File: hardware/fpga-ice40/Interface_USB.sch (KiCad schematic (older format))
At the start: 14 parts, among them J5 USB_B_Micro, U11 USBLC6-2SC6, U9 FT245RL

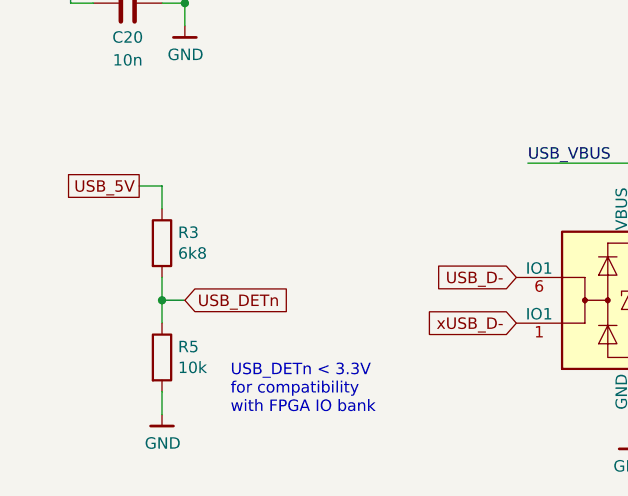
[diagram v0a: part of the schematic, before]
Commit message: Routed N64, DRAM, FIFO, and SD card interfaces
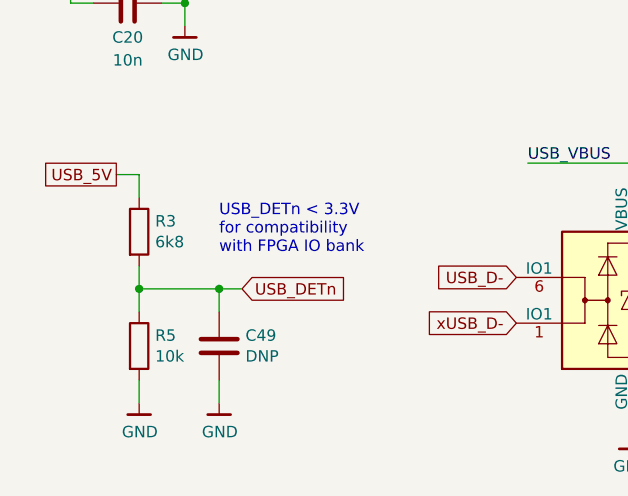
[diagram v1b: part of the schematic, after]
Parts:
- added C49: DNP, Capacitor_SMD:C_0603_1608Metric, symbol Device:C
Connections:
- net GND: now also C49.2
- net USB_DETn: now also C49.1
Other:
- moved on the sheet: R3, R5
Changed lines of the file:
@@
 L Device:R R?
 U 1 1 5F3148AD
-P 3150 4500
+P 3050 4450
 AR Path="/5F3148AD" Ref="R?"  Part="1"
 AR Path="/5F302051/5F3148AD" Ref="R3"  Part="1"
-F 0 "R3" H 3220 4546 50  0000 L CNN
-F 1 "6k8" H 3220 4455 50  0000 L CNN
-F 2 "Resistor_SMD:R_0603_1608Metric" V 3080 4500 50  0001 C CNN
-F 3 "~" H 3150 4500 50  0001 C CNN
-F 4 "RC0603FR-076K8L" H 3150 4500 50  0001 C CNN "MPN"
-	1    3150 4500
-	1    0    0    -1
-$EndComp
-$Comp
-L Device:R R?
-U 1 1 5F3148B3
-P 3150 5000
-AR Path="/5F3148B3" Ref="R?"  Part="1"
-AR Path="/5F302051/5F3148B3" Ref="R5"  Part="1"
-F 0 "R5" H 3220 5046 50  0000 L CNN
-F 1 "10k" H 3220 4955 50  0000 L CNN
-F 2 "Resistor_SMD:R_0603_1608Metric" V 3080 5000 50  0001 C CNN
-F 3 "~" H 3150 5000 50  0001 C CNN
-F 4 "RC0603FR-0710KL" H 3150 5000 50  0001 C CNN "MPN"
-	1    3150 5000
-	1    0    0    -1
-$EndComp
-Wire Wire Line
-	3150 5150 3150 5250
+F 0 "R3" H 3120 4496 50  0000 L CNN
+F 1 "6k8" H 3120 4405 50  0000 L CNN
+F 2 "Resistor_SMD:R_0603_1608Metric" V 2980 4450 50  0001 C CNN
+F 3 "~" H 3050 4450 50  0001 C CNN
+F 4 "RC0603FR-076K8L" H 3050 4450 50  0001 C CNN "MPN"
+	1    3050 4450
+	1    0    0    -1
+$EndComp
+Wire Wire Line
+	3050 5100 3050 5200
 $Comp
 L ng_power:GND #PWR?
 U 1 1 5F3148BA
-P 3150 5250
+P 3050 5200
 AR Path="/5F3148BA" Ref="#PWR?"  Part="1"
 AR Path="/5F302051/5F3148BA" Ref="#PWR024"  Part="1"
-F 0 "#PWR024" H 3150 5000 50  0001 C CNN
-F 1 "GND" H 3153 5124 50  0000 C CNN
-F 2 "" H 3050 4900 50  0001 C CNN
-F 3 "" H 3150 5250 50  0001 C CNN
-	1    3150 5250
-	1    0    0    -1
-$EndComp
-Wire Wire Line
-	3150 4650 3150 4750
-Wire Wire Line
-	3150 4350 3150 4250
-Wire Wire Line
-	3150 4250 3050 4250
-Wire Wire Line
-	3150 4750 3250 4750
-Connection ~ 3150 4750
-Wire Wire Line
-	3150 4750 3150 4850
-Text GLabel 3250 4750 2    50   Input ~ 0
+F 0 "#PWR024" H 3050 4950 50  0001 C CNN
+F 1 "GND" H 3053 5074 50  0000 C CNN
+F 2 "" H 2950 4850 50  0001 C CNN
+F 3 "" H 3050 5200 50  0001 C CNN
+	1    3050 5200
+	1    0    0    -1
+$EndComp
+Wire Wire Line
+	3050 4600 3050 4700
+Wire Wire Line
+	3050 4300 3050 4200
+Wire Wire Line
+	3050 4200 2950 4200
+Wire Wire Line
+	3050 4700 3400 4700
+Connection ~ 3050 4700
+Wire Wire Line
+	3050 4700 3050 4800
+Text GLabel 3500 4700 2    50   Input ~ 0
 USB_DETn
 $Comp
@@
 Text GLabel 4800 2450 2    50   UnSpc ~ 0
 USB_5V
-Text GLabel 3050 4250 0    50   UnSpc ~ 0
+Text GLabel 2950 4200 0    50   UnSpc ~ 0
 USB_5V
 $Comp
@@
 Text Label 3250 2450 0    50   ~ 0
 USB_VBUS
-Text Notes 3450 5250 0    50   ~ 0
+Text Notes 3400 4550 0    50   ~ 0
 USB_DETn < 3.3V\nfor compatibility\nwith FPGA IO bank
 $Comp
@@
 Wire Wire Line
 	4700 2450 4800 2450
+Wire Wire Line
+	3400 4800 3400 4700
+Connection ~ 3400 4700
+Wire Wire Line
+	3400 4700 3500 4700
+Wire Wire Line
+	3400 5100 3400 5200
+$Comp
+L ng_power:GND #PWR?
+U 1 1 5F312C25
+P 3400 5200
+AR Path="/5F312C25" Ref="#PWR?"  Part="1"
+AR Path="/5F302051/5F312C25" Ref="#PWR039"  Part="1"
+F 0 "#PWR039" H 3400 4950 50  0001 C CNN
+F 1 "GND" H 3403 5074 50  0000 C CNN
+F 2 "" H 3300 4850 50  0001 C CNN
+F 3 "" H 3400 5200 50  0001 C CNN
+	1    3400 5200
+	1    0    0    -1
+$EndComp
+$Comp
+L Device:R R?
+U 1 1 5F3148B3
+P 3050 4950
+AR Path="/5F3148B3" Ref="R?"  Part="1"
+AR Path="/5F302051/5F3148B3" Ref="R5"  Part="1"
+F 0 "R5" H 3120 4996 50  0000 L CNN
+F 1 "10k" H 3120 4905 50  0000 L CNN
+F 2 "Resistor_SMD:R_0603_1608Metric" V 2980 4950 50  0001 C CNN
+F 3 "~" H 3050 4950 50  0001 C CNN
+F 4 "RC0603FR-0710KL" H 3050 4950 50  0001 C CNN "MPN"
+	1    3050 4950
+	1    0    0    -1
+$EndComp
+$Comp
+L Device:C C49
+U 1 1 5F31C8F6
+P 3400 4950
+F 0 "C49" H 3515 4996 50  0000 L CNN
+F 1 "DNP" H 3515 4905 50  0000 L CNN
+F 2 "Capacitor_SMD:C_0603_1608Metric" H 3438 4800 50  0001 C CNN
+F 3 "~" H 3400 4950 50  0001 C CNN
+	1    3400 4950
+	1    0    0    -1
+$EndComp
 $EndSCHEMATC

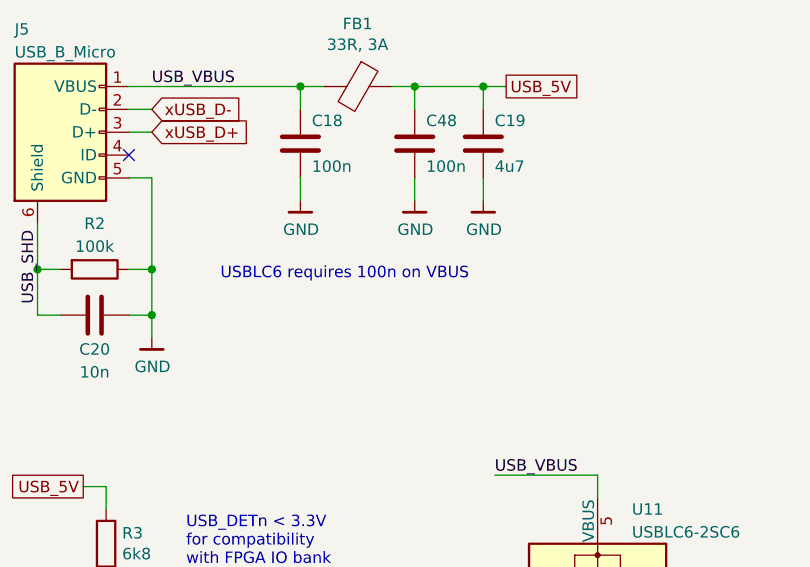
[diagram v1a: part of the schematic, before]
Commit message: Fix two misrouted power traces in USB section
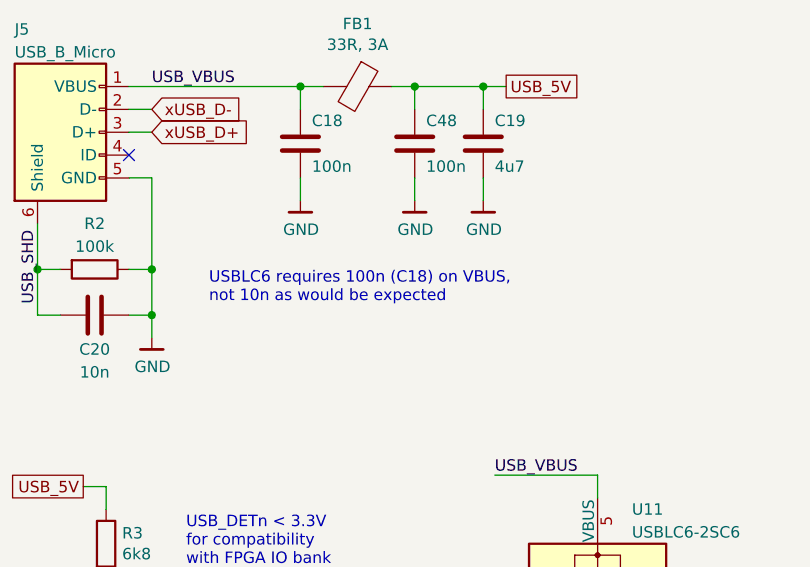
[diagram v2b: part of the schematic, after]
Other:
- note added: "USBLC6 requires 100n (C18) on VBUS,\nnot 10n as would be expected"
- note removed: "USBLC6 requires 100n on VBUS"
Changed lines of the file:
@@
 Text Label 4750 4150 0    50   ~ 0
 USB_VBUS
-Text Notes 3550 3300 0    50   ~ 0
-USBLC6 requires 100n on VBUS
+Text Notes 3500 3400 0    50   ~ 0
+USBLC6 requires 100n (C18) on VBUS,\nnot 10n as would be expected
 Wire Wire Line
 	4300 2450 4400 2450

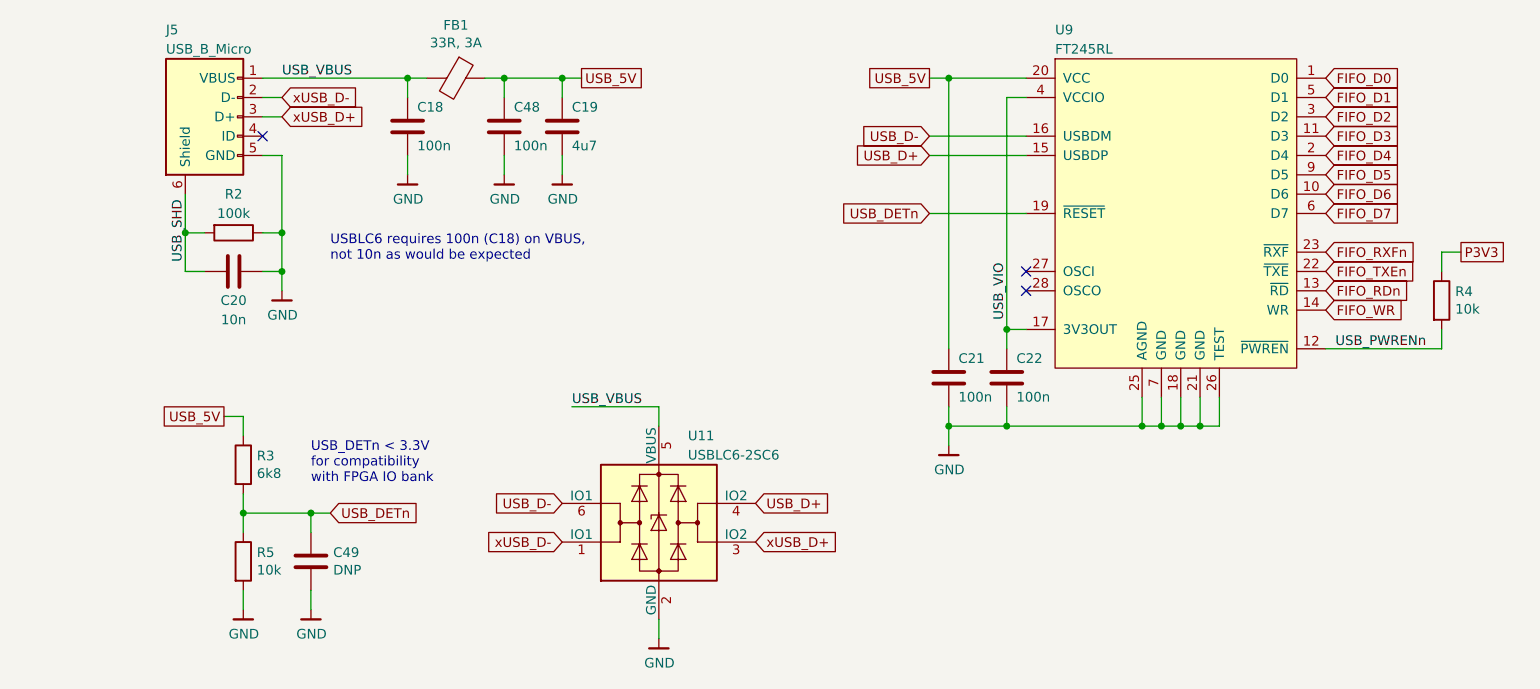
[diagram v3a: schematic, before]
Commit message: Confirmed controlled impedance and decoupling specifications
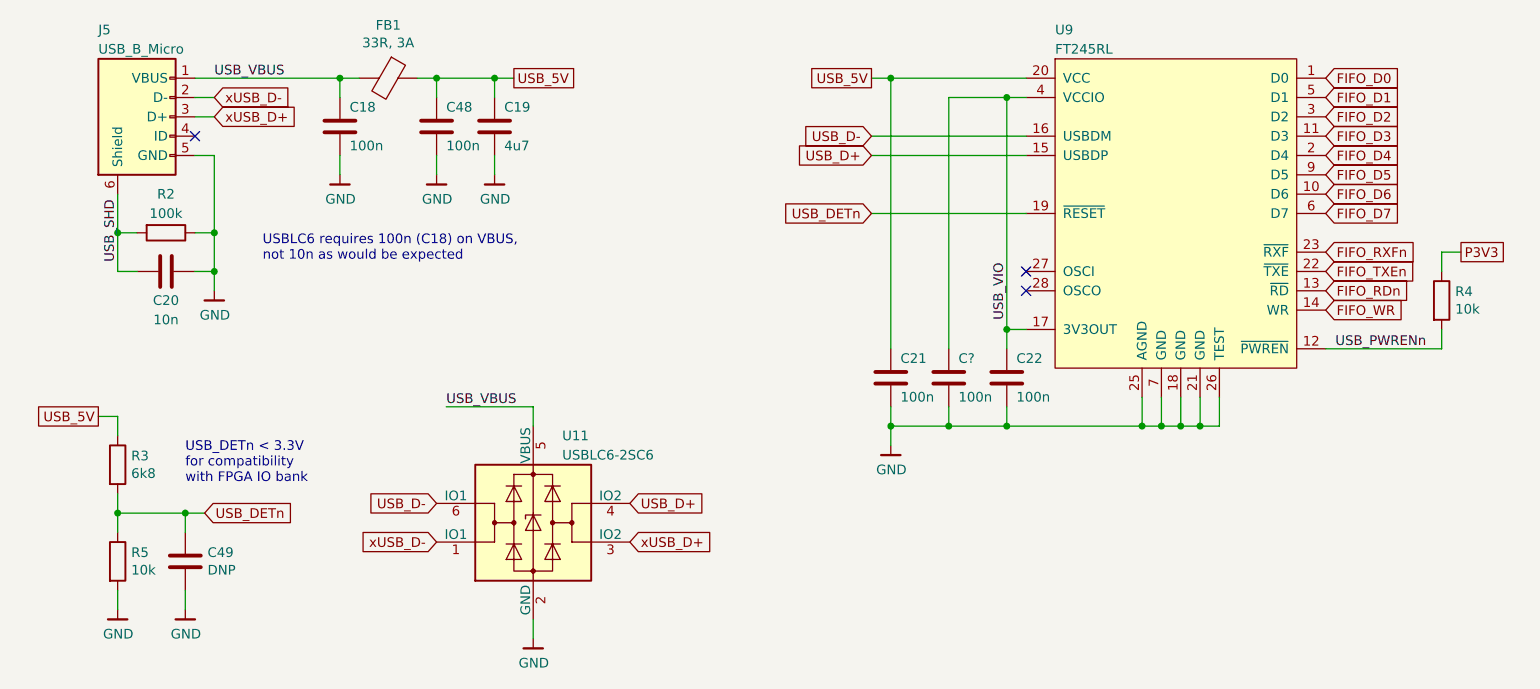
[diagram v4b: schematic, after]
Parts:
- added C?: 100n, Capacitor_SMD:C_0603_1608Metric, symbol Device:C
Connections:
- net GND: now also C?.2
- net USB_VIO: now also C?.1
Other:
- moved on the sheet: C18, C19, C20, C21, C48, C49, FB1, J5, R2, R3, R5, U11
